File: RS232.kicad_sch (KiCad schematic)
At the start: 10 parts, among them U5 SP3232EEN-L/TR

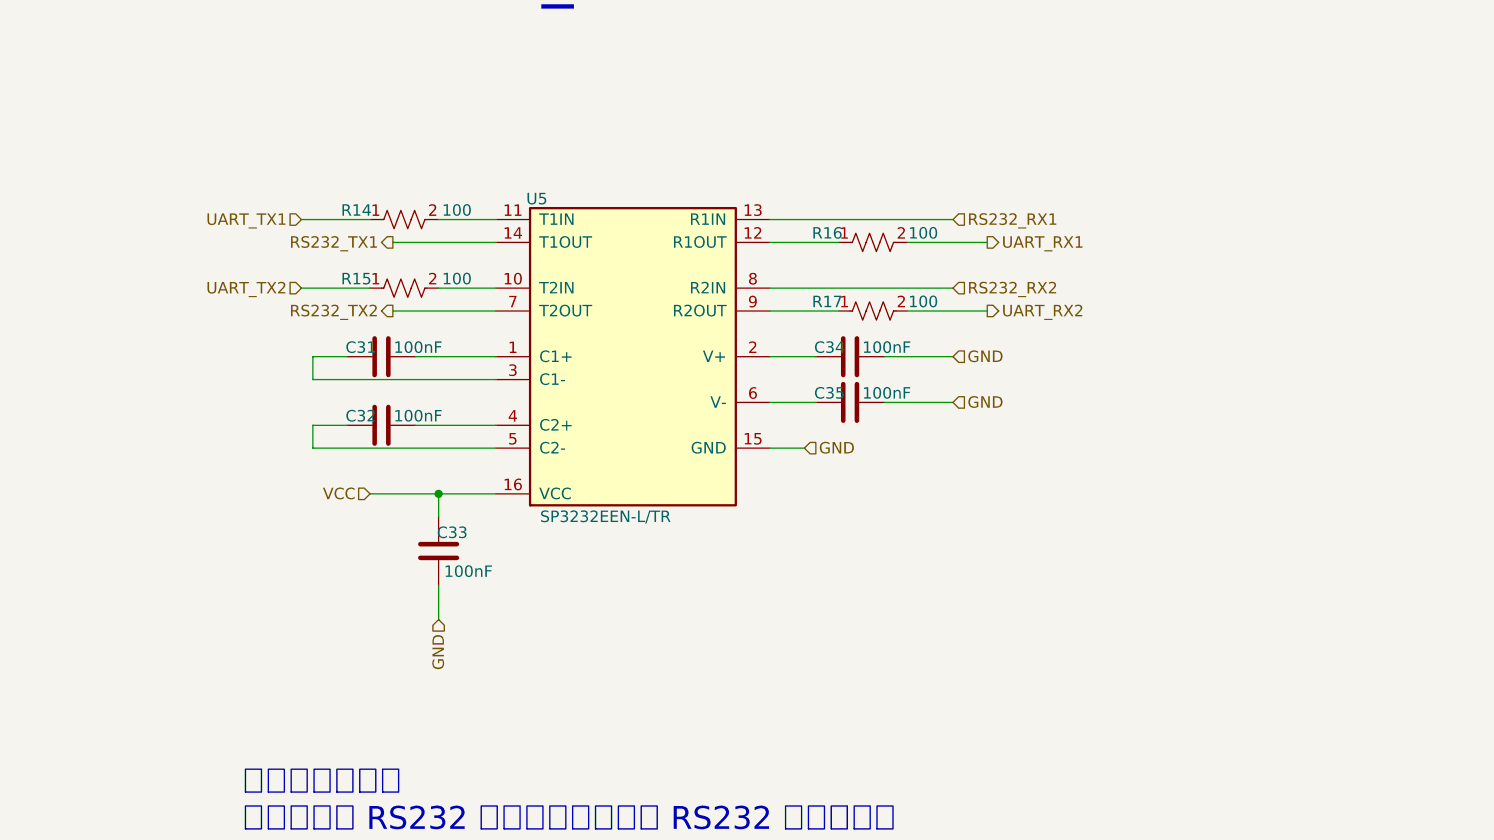
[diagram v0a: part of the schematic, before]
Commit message: 增加USB,TYPEC转串口esd隔离，
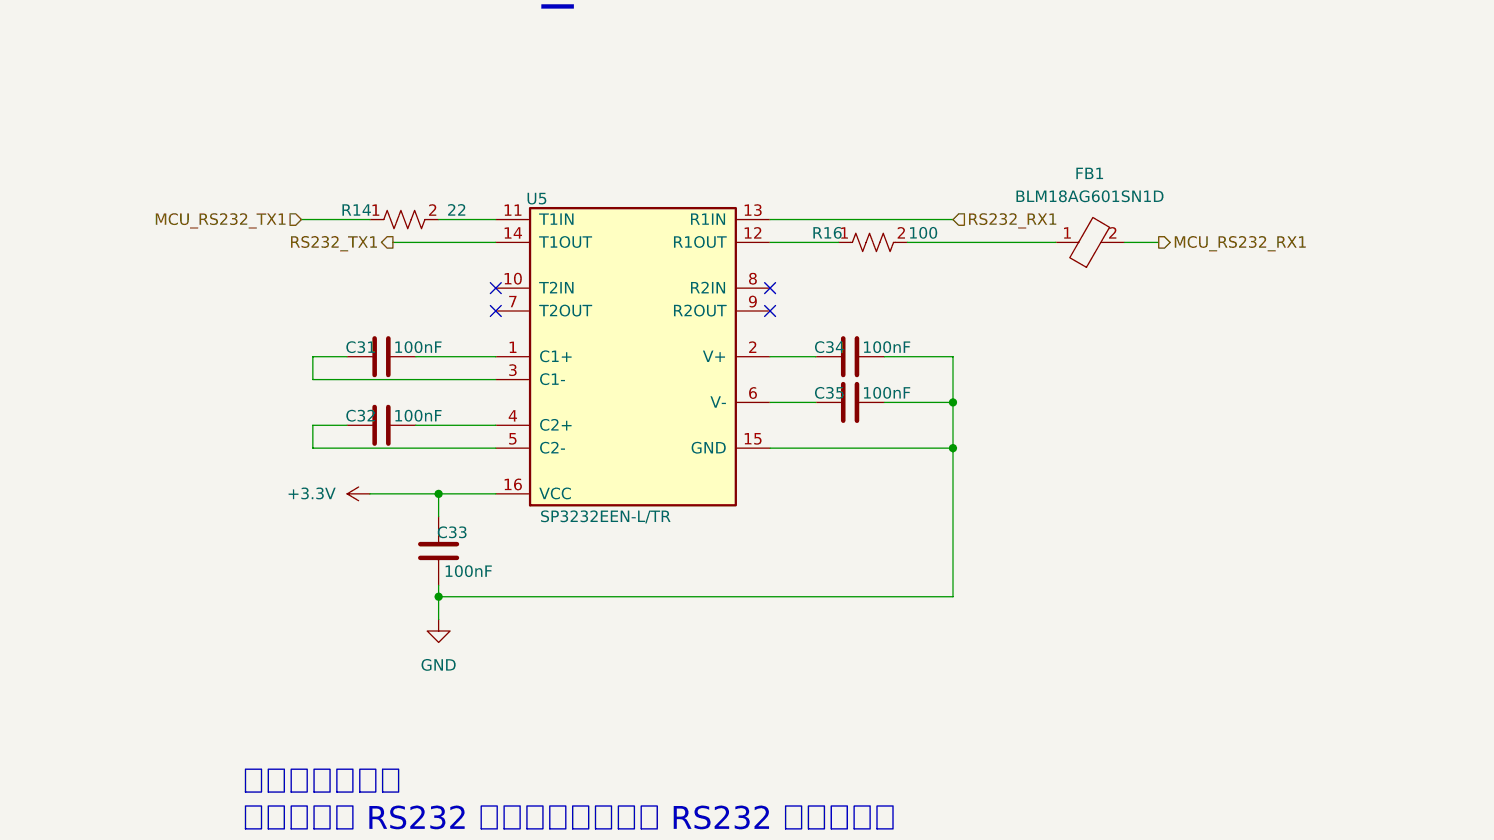
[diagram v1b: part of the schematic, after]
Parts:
- removed R15, R17: 100, kicad_api_lib:TC0525F1000T5E, symbol TC0525F1000T5E:TC0525F1000T5E
- added FB1: BLM18AG601SN1D, kicad_api_lib:BLM18AG601SN1D, symbol BLM18AG601SN1D:FerriteBead
- R14: value 100 -> 22
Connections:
- net RS232_RX2: no longer names the net of U5.8 (R2IN)
- net RS232_TX2: no longer names the net of U5.7 (T2OUT)
- net UART_RX1: no longer names the net of R16.2
- net UART_RX1: now also FB1.1
- net UART_TX1 renamed MCU_RS232_TX1
- net VCC renamed +3.3V
- new net MCU_RS232_RX1: FB1.2
- no-connect marks 0 -> 4

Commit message: 完成GD32F303控制板原理图与PCB设计
- 更新电源、CAN、RS232、RS485及电机通信子电路
- 切换并完善GD32F303VCT6核心原理图
- 新增PCB布局及所需符号、封装库文件
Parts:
- added CN4: WJ15EDGRC-3.81-2P, kicad_api_lib:WJ15EDGRC-3.81-2P, symbol WJ15EDGRC-3.81-2P:31330102
- C37: renamed from C31; footprint kicad_api_lib:0603B104K500CT -> Capacitor_SMD:C_0201_0603Metric_Pad0.64x0.40mm_HandSolder
- C38: renamed from C32; footprint kicad_api_lib:0603B104K500CT -> Capacitor_SMD:C_0201_0603Metric_Pad0.64x0.40mm_HandSolder
- C39: renamed from C33; footprint kicad_api_lib:0603B104K500CT -> Capacitor_SMD:C_0201_0603Metric_Pad0.64x0.40mm_HandSolder
- C40: renamed from C34; footprint kicad_api_lib:0603B104K500CT -> Capacitor_SMD:C_0201_0603Metric_Pad0.64x0.40mm_HandSolder
- C41: renamed from C35; footprint kicad_api_lib:0603B104K500CT -> Capacitor_SMD:C_0201_0603Metric_Pad0.64x0.40mm_HandSolder
- R14: footprint kicad_api_lib:TC0525F1000T5E -> Resistor_SMD:R_0805_2012Metric_Pad1.20x1.40mm_HandSolder
- R15: renamed from R16; footprint kicad_api_lib:TC0525F1000T5E -> Resistor_SMD:R_0805_2012Metric_Pad1.20x1.40mm_HandSolder
- U8: renamed from U5; footprint kicad_api_lib:SP3232EEN-L_TR -> Package_SO:SOIC-16_3.9x9.9mm_P1.27mm
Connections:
- net RS232_RX1: now also CN4.1
- net RS232_TX1: now also CN4.2

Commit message: 优化接口原理图与PCB布局
- 精简CAN接口并调整各子页器件编号
- 更新电源输入端子与Type-C接口封装
- 重新整理控制板PCB器件布局
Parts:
- C37, C38, C39, C40, C41, FB1, R14, R15, U8: now not fitted
- CN3: renamed from CN4; now not fitted
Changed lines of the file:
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@@
 		(on_board yes)
 		(in_pos_files yes)
-		(dnp no)
+		(dnp yes)
 		(property "Reference" "R15"
 			(at 158.75 76.454 90)
@@
 		(on_board yes)
 		(in_pos_files yes)
-		(dnp no)
+		(dnp yes)
 		(property "Reference" "R14"
 			(at 106.426 73.914 90)
@@
 		(on_board yes)
 		(in_pos_files yes)
-		(dnp no)
+		(dnp yes)
 		(fields_autoplaced yes)
-		(property "Reference" "CN4"
+		(property "Reference" "CN3"
 			(at 234.95 91.4399 90)
 			(show_name no)
@@
 			(project "GD32F303"
 				(path "/54005433-e3aa-4693-8f75-bb73943288d3/6d57bf2a-6797-463e-a7be-460e5ac424fd"
-					(reference "CN4")
+					(reference "CN3")
 					(unit 1)
 				)
@@
 		(on_board yes)
 		(in_pos_files yes)
-		(dnp no)
+		(dnp yes)
 		(property "Reference" "U8"
 			(at 126.492 72.644 0)
@@
 		(on_board yes)
 		(in_pos_files yes)
-		(dnp no)
+		(dnp yes)
 		(property "Reference" "C41"
 			(at 159.004 94.234 90)
@@
 		(on_board yes)
 		(in_pos_files yes)
-		(dnp no)
+		(dnp yes)
 		(property "Reference" "C38"
 			(at 106.934 96.774 90)
@@
 		(on_board yes)
 		(in_pos_files yes)
-		(dnp no)
+		(dnp yes)
 		(property "Reference" "C39"
 			(at 117.094 109.728 0)
@@
 		(on_board yes)
 		(in_pos_files yes)
-		(dnp no)
+		(dnp yes)
 		(property "Reference" "C37"
 			(at 106.934 89.154 90)
@@
 		(on_board yes)
 		(in_pos_files yes)
-		(dnp no)
+		(dnp yes)
 		(fields_autoplaced yes)
 		(property "Reference" "FB1"
@@
 		(on_board yes)
 		(in_pos_files yes)
-		(dnp no)
+		(dnp yes)
 		(property "Reference" "C40"
 			(at 159.004 89.154 90)

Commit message: 完善总线映射并划分隔离地与电源平面
统一3V3电源网络并消除ERC错误；优化GND/Earth耦合器件布局；完成In1.Cu地平面及In2.Cu电源平面分区。
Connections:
- net +3.3V renamed +3V3
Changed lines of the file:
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@@
 			)
 		)
-		(property "Value" "+3.3V"
+		(property "Value" "+3V3"
 			(at 104.14 105.4099 90)
 			(show_name no)

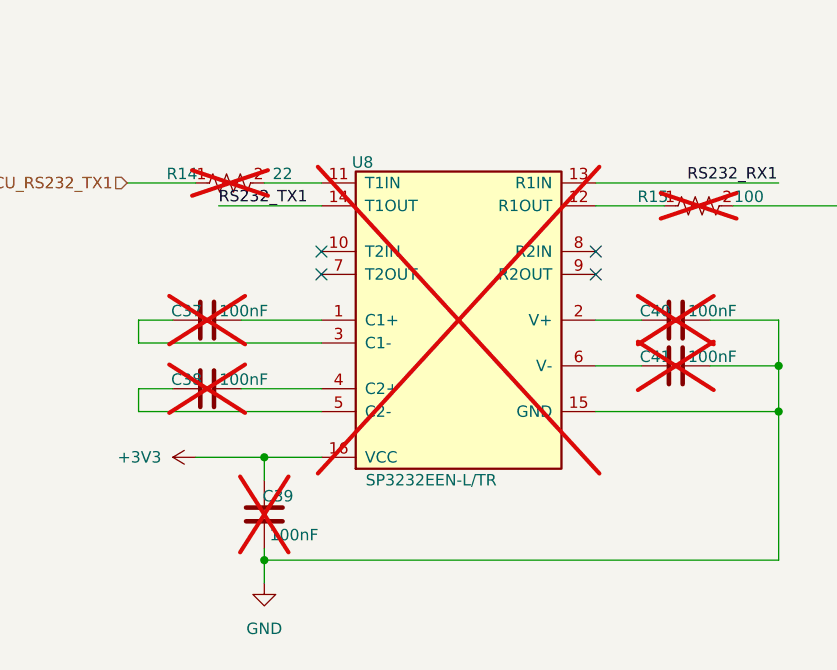
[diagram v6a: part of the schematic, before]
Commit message: 更新六层控制板设计及嘉立创生产文件
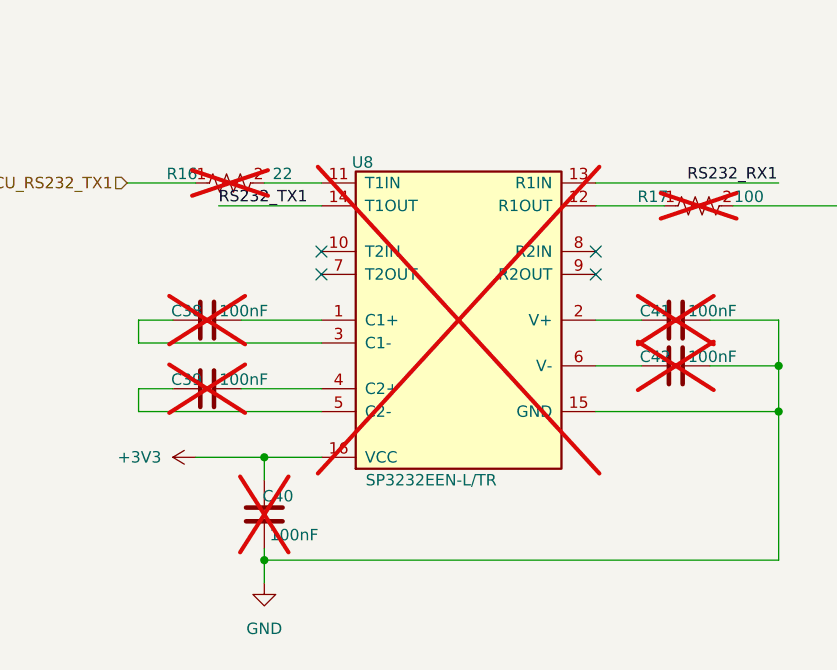
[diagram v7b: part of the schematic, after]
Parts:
- renumbered C37 to C38, C38 to C39, C39 to C40, C40 to C41, C41 to C42, R14 to R16, R15 to R17
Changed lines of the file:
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@@
 		(in_pos_files no)
 		(dnp yes)
-		(property "Reference" "R15"
+		(property "Reference" "R17"
 			(at 158.75 76.454 90)
 			(show_name no)
@@
 			(project "GD32F303VET6_4Motor_Control"
 				(path "/54005433-e3aa-4693-8f75-bb73943288d3/6d57bf2a-6797-463e-a7be-460e5ac424fd"
-					(reference "R15")
+					(reference "R17")
 					(unit 1)
 				)
@@
 		(in_pos_files no)
 		(dnp yes)
-		(property "Reference" "R14"
+		(property "Reference" "R16"
 			(at 106.426 73.914 90)
 			(show_name no)
@@
 			(project "GD32F303VET6_4Motor_Control"
 				(path "/54005433-e3aa-4693-8f75-bb73943288d3/6d57bf2a-6797-463e-a7be-460e5ac424fd"
-					(reference "R14")
+					(reference "R16")
 					(unit 1)
 				)
@@
 		(in_pos_files no)
 		(dnp yes)
-		(property "Reference" "C41"
+		(property "Reference" "C42"
 			(at 159.004 94.234 90)
 			(show_name no)
@@
 			(project "GD32F303VET6_4Motor_Control"
 				(path "/54005433-e3aa-4693-8f75-bb73943288d3/6d57bf2a-6797-463e-a7be-460e5ac424fd"
-					(reference "C41")
+					(reference "C42")
 					(unit 1)
 				)
@@
 		(in_pos_files no)
 		(dnp yes)
-		(property "Reference" "C38"
+		(property "Reference" "C39"
 			(at 106.934 96.774 90)
 			(show_name no)
@@
 			(project "GD32F303VET6_4Motor_Control"
 				(path "/54005433-e3aa-4693-8f75-bb73943288d3/6d57bf2a-6797-463e-a7be-460e5ac424fd"
-					(reference "C38")
+					(reference "C39")
 					(unit 1)
 				)
@@
 		(in_pos_files no)
 		(dnp yes)
-		(property "Reference" "C39"
+		(property "Reference" "C40"
 			(at 117.094 109.728 0)
 			(show_name no)
@@
 			(project "GD32F303VET6_4Motor_Control"
 				(path "/54005433-e3aa-4693-8f75-bb73943288d3/6d57bf2a-6797-463e-a7be-460e5ac424fd"
-					(reference "C39")
+					(reference "C40")
 					(unit 1)
 				)
@@
 		(dnp no)
 		(fields_autoplaced yes)
-		(property "Reference" "#PWR051"
+		(property "Reference" "#PWR057"
 			(at 111.76 105.41 0)
 			(hide yes)
@@
 			(project "GD32F303VET6_4Motor_Control"
 				(path "/54005433-e3aa-4693-8f75-bb73943288d3/6d57bf2a-6797-463e-a7be-460e5ac424fd"
-					(reference "#PWR051")
+					(reference "#PWR057")
 					(unit 1)
 				)
@@
 		(in_pos_files no)
 		(dnp yes)
-		(property "Reference" "C37"
+		(property "Reference" "C38"
 			(at 106.934 89.154 90)
 			(show_name no)
@@
 			(project "GD32F303VET6_4Motor_Control"
 				(path "/54005433-e3aa-4693-8f75-bb73943288d3/6d57bf2a-6797-463e-a7be-460e5ac424fd"
-					(reference "C37")
+					(reference "C38")
 					(unit 1)
 				)
@@
 		(in_pos_files no)
 		(dnp yes)
-		(property "Reference" "C40"
+		(property "Reference" "C41"
 			(at 159.004 89.154 90)
 			(show_name no)
@@
 			(project "GD32F303VET6_4Motor_Control"
 				(path "/54005433-e3aa-4693-8f75-bb73943288d3/6d57bf2a-6797-463e-a7be-460e5ac424fd"
-					(reference "C40")
+					(reference "C41")
 					(unit 1)
 				)
@@
 		(dnp no)
 		(fields_autoplaced yes)
-		(property "Reference" "#PWR052"
+		(property "Reference" "#PWR058"
 			(at 115.57 125.73 0)
 			(hide yes)
@@
 			(project "GD32F303VET6_4Motor_Control"
 				(path "/54005433-e3aa-4693-8f75-bb73943288d3/6d57bf2a-6797-463e-a7be-460e5ac424fd"
-					(reference "#PWR052")
+					(reference "#PWR058")
 					(unit 1)
 				)

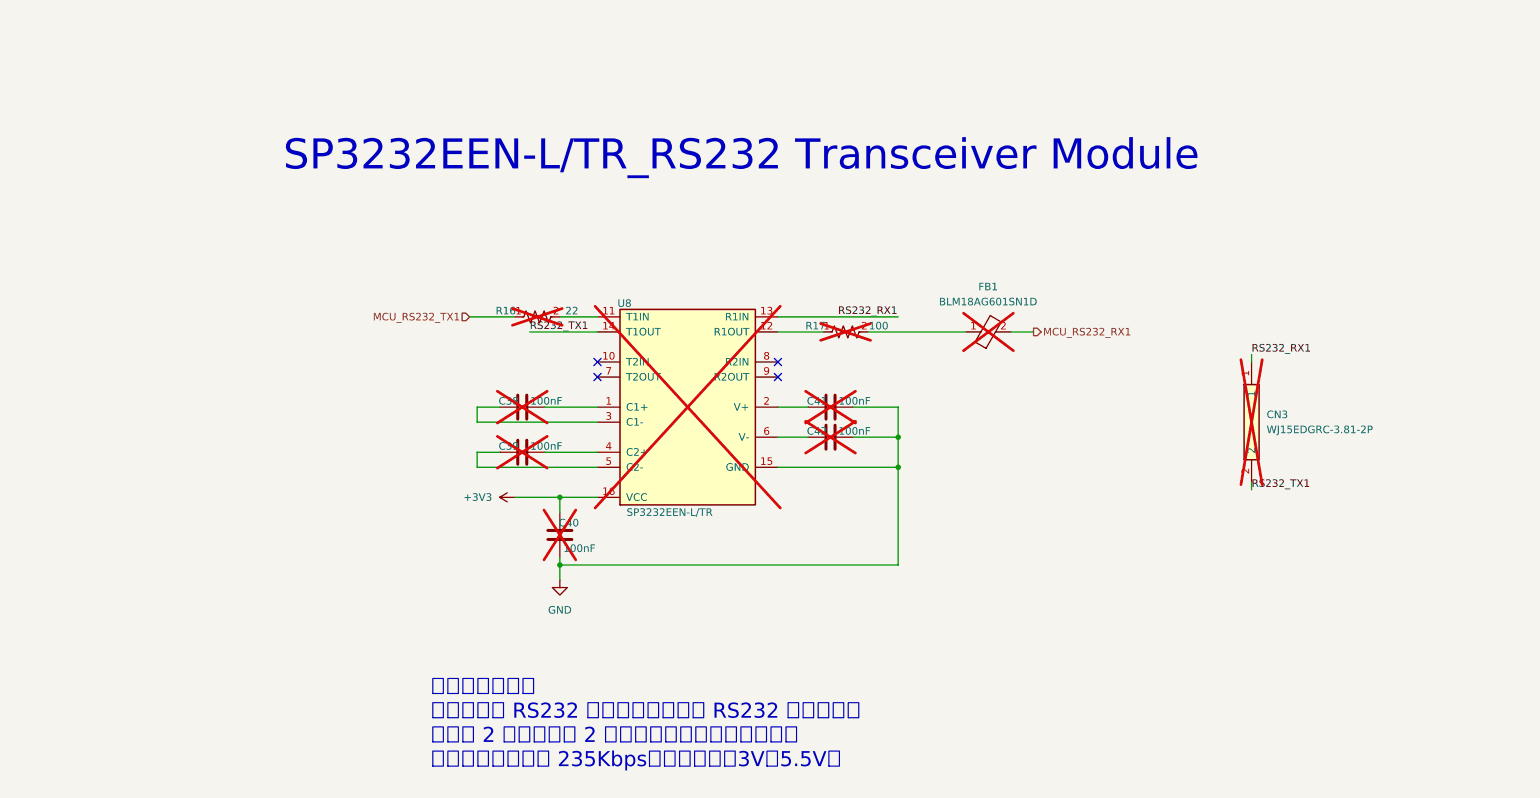
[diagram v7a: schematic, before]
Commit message: V2.0: sync KiCad design, add firmware snapshot and README
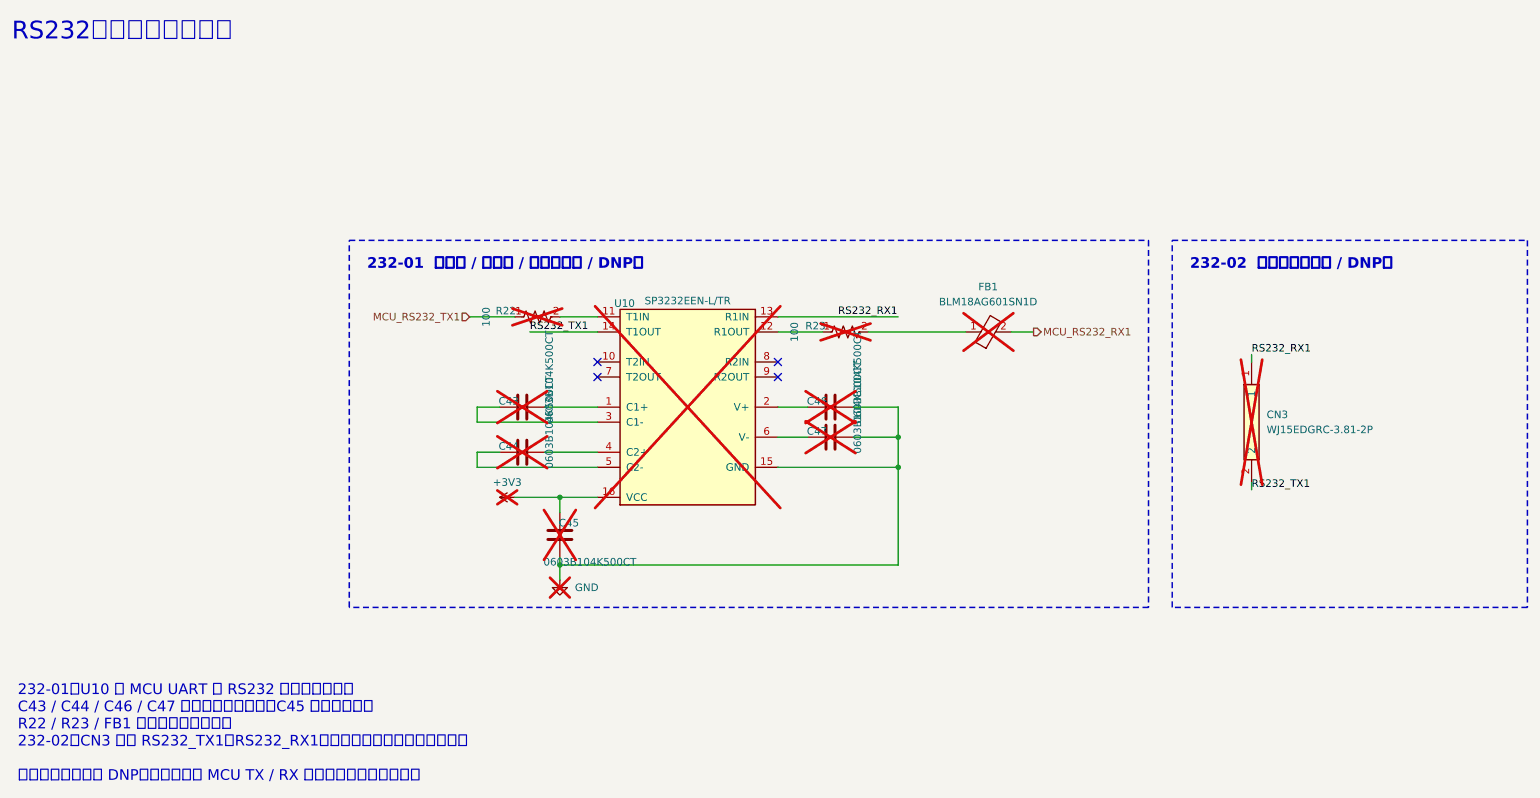
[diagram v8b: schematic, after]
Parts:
- C43: renamed from C38; value 100nF -> 0603B104K500CT; footprint Capacitor_SMD:C_0201_0603Metric_Pad0.64x0.40mm_HandSolder -> Capacitor_SMD:C_0603_1608Metric; now left out of the parts list
- C44: renamed from C39; value 100nF -> 0603B104K500CT; footprint Capacitor_SMD:C_0201_0603Metric_Pad0.64x0.40mm_HandSolder -> Capacitor_SMD:C_0603_1608Metric; now left out of the parts list
- C45: renamed from C40; value 100nF -> 0603B104K500CT; footprint Capacitor_SMD:C_0201_0603Metric_Pad0.64x0.40mm_HandSolder -> Capacitor_SMD:C_0603_1608Metric; now left out of the parts list
- C46: renamed from C41; value 100nF -> 0603B104K500CT; footprint Capacitor_SMD:C_0201_0603Metric_Pad0.64x0.40mm_HandSolder -> Capacitor_SMD:C_0603_1608Metric; now left out of the parts list
- C47: renamed from C42; value 100nF -> 0603B104K500CT; footprint Capacitor_SMD:C_0201_0603Metric_Pad0.64x0.40mm_HandSolder -> Capacitor_SMD:C_0603_1608Metric; now left out of the parts list
- CN3, FB1: now left out of the parts list
- R22: renamed from R16; value 22 -> 100; footprint Resistor_SMD:R_0805_2012Metric_Pad1.20x1.40mm_HandSolder -> Resistor_SMD:R_0603_1608Metric; symbol TC0525F1000T5E:TC0525F1000T5E -> Project_Passives:ERJPA3F1000V_a825e2f2; MPN TC0525F1000T5E -> ERJPA3F1000V; Manufacturer Royal Electronic Factory -> Panasonic; Power (none) -> 0.33W; Resistance (none) -> 100; Tolerance (none) -> 1%; huaqiu_pn G6464272 -> (none); operating_temperature -55 °C -> (none); overload_voltage 150 V -> (none); package 0805 -> 0603; power_rating 250 mW -> (none); temperature_coefficient 25 ppm/°C -> (none); tolerance 1 % -> (none); now left out of the parts list
- R23: renamed from R17; footprint Resistor_SMD:R_0805_2012Metric_Pad1.20x1.40mm_HandSolder -> Resistor_SMD:R_0603_1608Metric; symbol TC0525F1000T5E:TC0525F1000T5E -> Project_Passives:ERJPA3F1000V_a825e2f2; MPN TC0525F1000T5E -> ERJPA3F1000V; Manufacturer Royal Electronic Factory -> Panasonic; Power (none) -> 0.33W; Resistance (none) -> 100; Tolerance (none) -> 1%; huaqiu_pn G6464272 -> (none); operating_temperature -55 °C -> (none); overload_voltage 150 V -> (none); package 0805 -> 0603; power_rating 250 mW -> (none); temperature_coefficient 25 ppm/°C -> (none); tolerance 1 % -> (none); now left out of the parts list
- U10: renamed from U8; footprint Package_SO:SOIC-16_3.9x9.9mm_P1.27mm -> kicad_api_lib:SP3232EEN-L_TR; now left out of the parts list
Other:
- note added: "232-01 收发器 / 电荷泵 / 滤波【备用 / DNP】"
- note added: "232-01：U10 将 MCU UART 与 RS232 电平互相转换。 C43 / C44 / C46 / C47 为电荷泵相关电容；C45 为电源去耦。 R22 / R23 / FB1 为串联阻抗及滤波。 232-02：CN3 引出 RS232_TX1、RS232_RX1，外接设备需具备共同参考地。 本页器件当前均为 DNP；启用前复核 MCU TX / RX 的实际收发方向与接线。"
- note added: "232-02 对外串口【备用 / DNP】"
- note added: "RS232｜备用不装配接口"
- note removed: "SP3232EEN-L/TR_RS232 Transceiver Module"
- note removed: "模块电路功能： 一款高性能 RS232 收发器芯片，采用 RS232 通信协议。 集成了 2 个驱动器和 2 个接收器，支持全双工通信。 数据速率最高可达 235Kbps，工作电压为3V至5.5V。"
